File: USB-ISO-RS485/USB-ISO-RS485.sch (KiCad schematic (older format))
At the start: 36 parts, among them P1 RS485 Connector, P10 TST, P11 TST, P12 TST, P13 UART Interface, P2 USB_A, P3 TST, P4 TST, P5 TST, P6 TST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

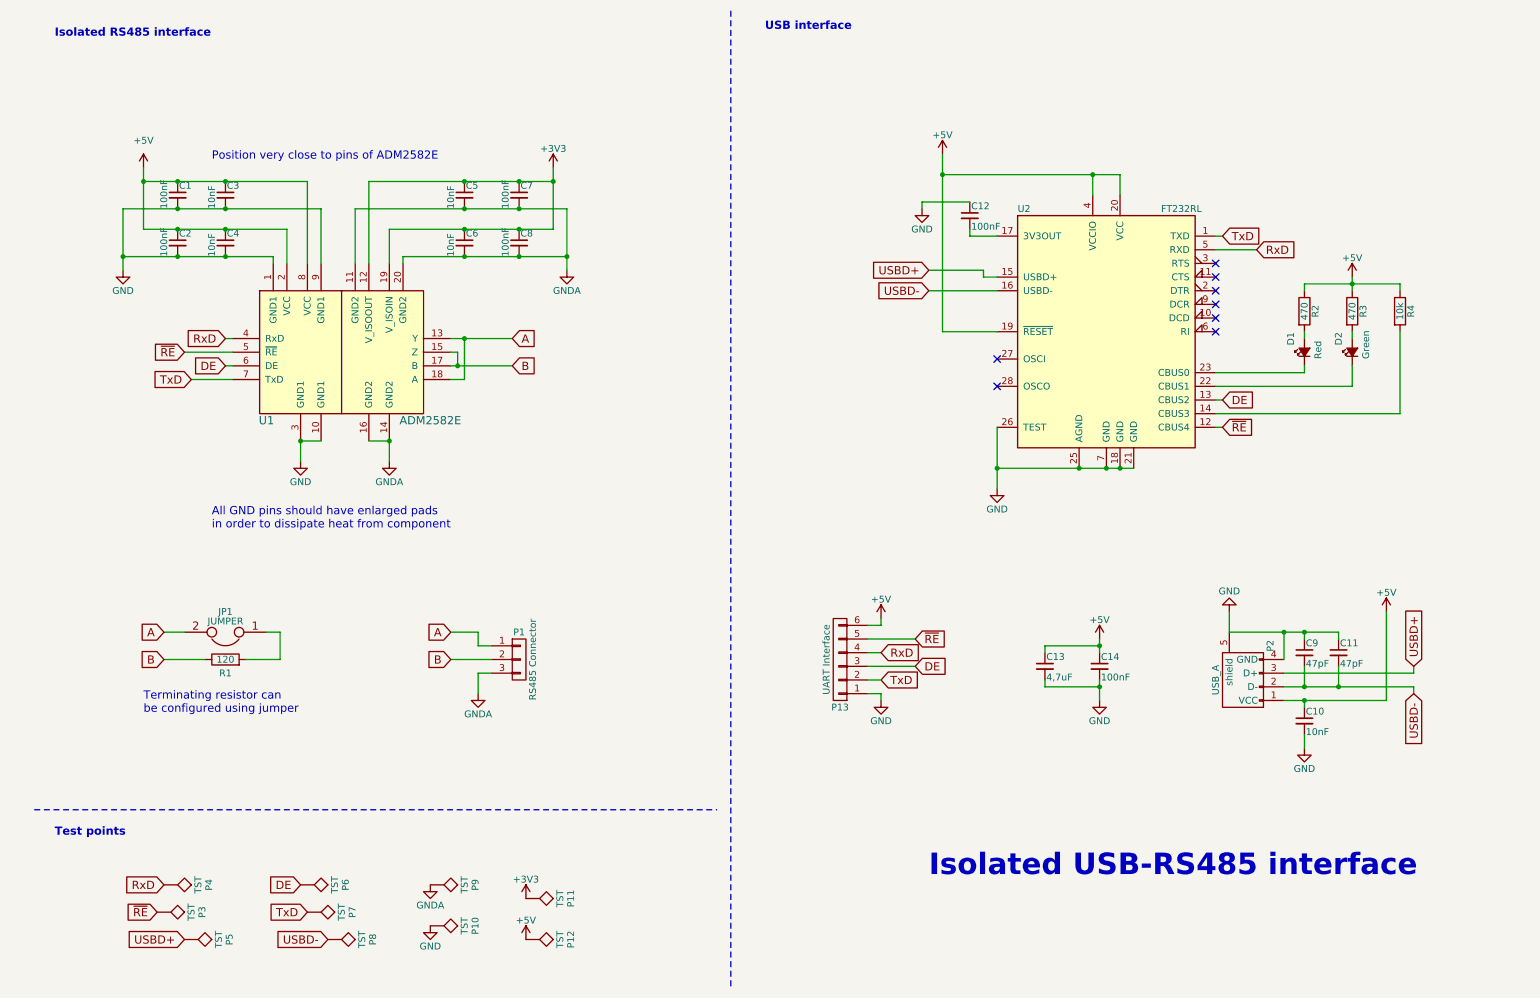
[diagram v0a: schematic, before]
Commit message: assigned all footprints
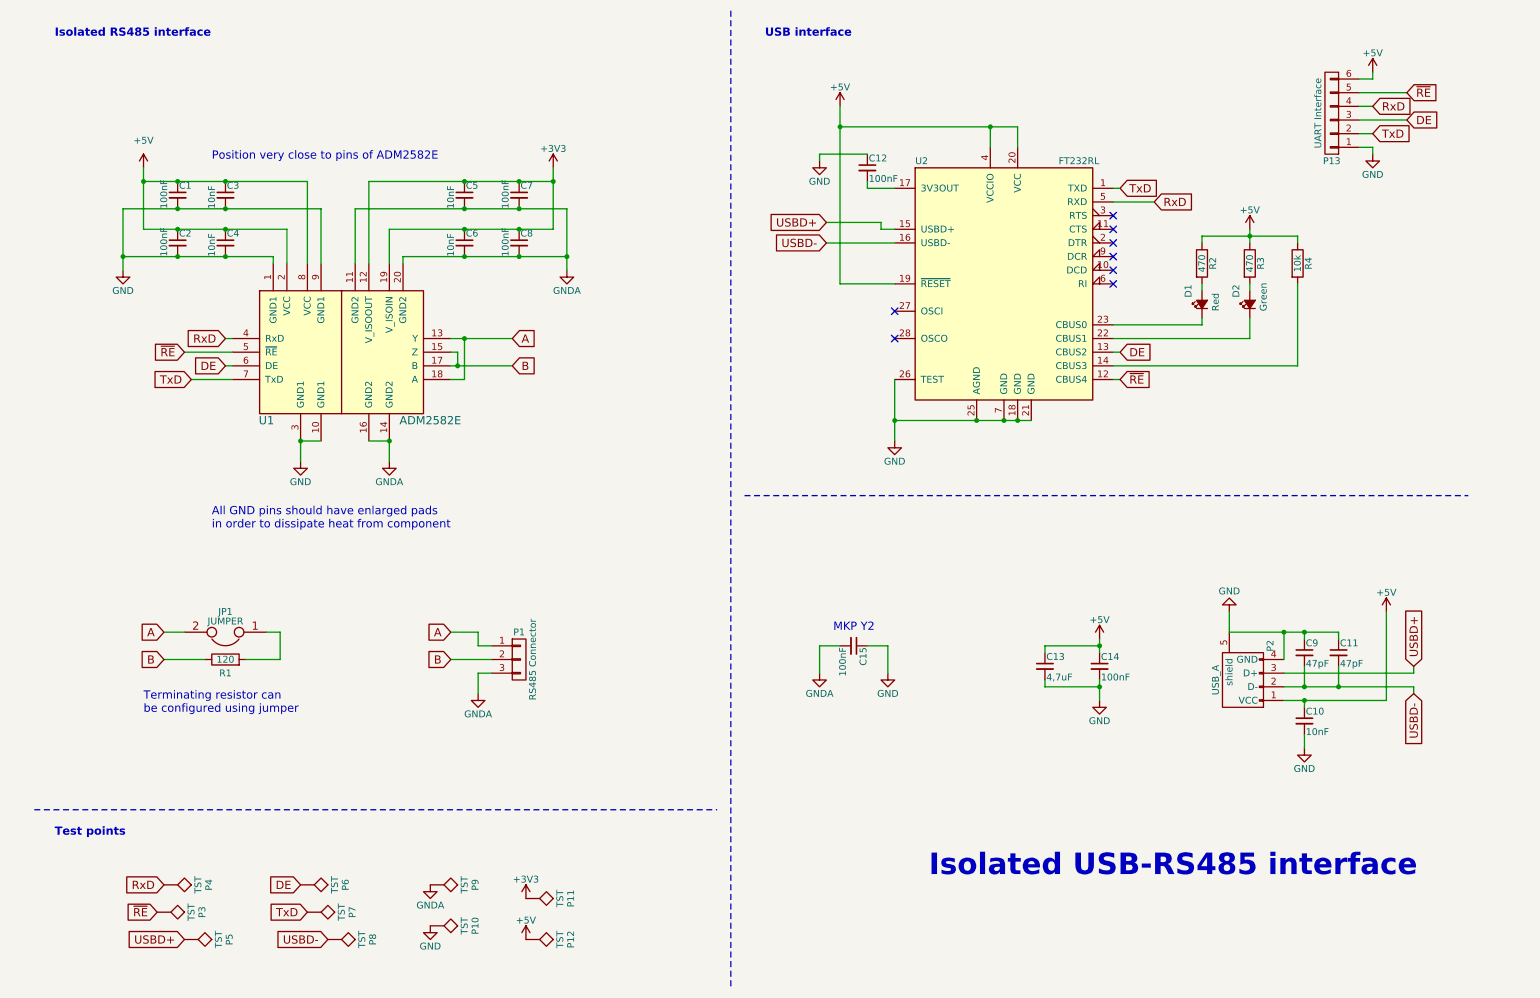
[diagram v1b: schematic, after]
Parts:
- added C15: 100nF, Capacitors_THT:C_Rect_L26.5mm_W7.0mm_P22.50mm_MKS4, symbol C_Small
- C1, C10, C11, C12, C13, C14, C2, C3, C4, C5, C6, C7, C8, C9: footprint (none) -> Capacitors_SMD:C_0805_HandSoldering
- D1, D2: footprint (none) -> LEDs:LED_0805
- JP1: footprint (none) -> Pin_Headers:Pin_Header_Straight_1x02_Pitch2.54mm
- P1: footprint (none) -> Connectors_WAGO:WAGO_734_3pin_Straight_RuggedPads
- P10, P11, P12, P3, P4, P5, P6, P7, P8, P9: footprint (none) -> Measurement_Points:Test_Point_Keystone_5010-5014_Multipurpose
- P13: footprint (none) -> Pin_Headers:Pin_Header_Straight_1x06_Pitch2.54mm
- P2: footprint (none) -> Connectors:USB_B
- R1, R2, R3, R4: footprint (none) -> Resistors_SMD:R_0805_HandSoldering
- U1: footprint Housings_SOIC:SOIC-20W_7.5x12.8mm_Pitch1.27mm -> ADM2582E:ADM2582E-SOIC20W-Thermal
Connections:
- net GND: now also C15.1
- net GNDA: now also C15.2
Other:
- note added: "MKP Y2"
- moved on the sheet: C12, D1, D2, P13, R2, R3, R4, U2

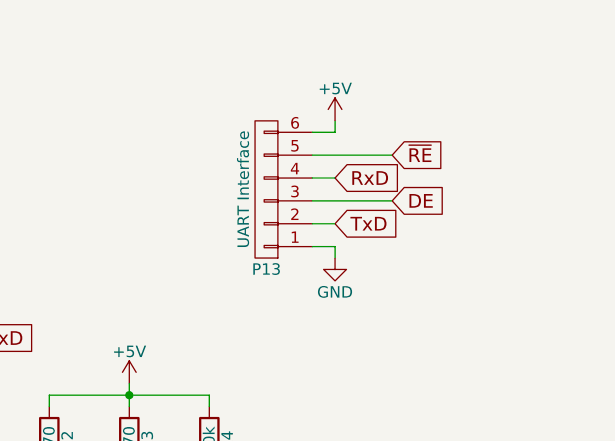
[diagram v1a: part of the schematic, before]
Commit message: broken layout - ADM2582E footprint to narrow
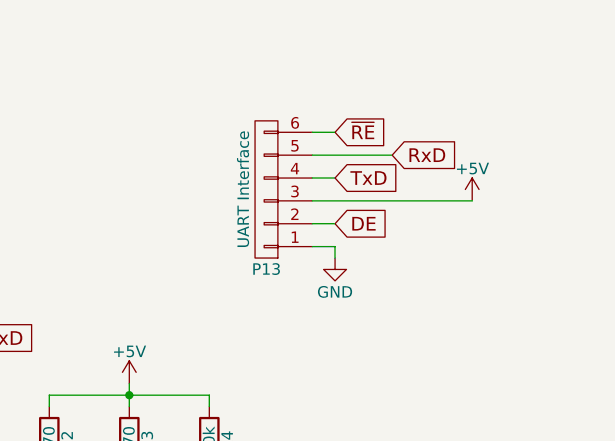
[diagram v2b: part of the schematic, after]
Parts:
- P10, P11, P12, P3, P4, P5, P6, P7, P8, P9: footprint Measurement_Points:Test_Point_Keystone_5010-5014_Multipurpose -> Measurement_Points:Measurement_Point_Round-TH_Small
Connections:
- net +5V: now also P13.3 (P3); no longer P13.6 (P6)
- net DE: now also P13.2 (P2); no longer P13.3 (P3)
- net RxD: now also P13.5 (P5); no longer P13.4 (P4)
- net TxD: now also P13.4 (P4); no longer P13.2 (P2)
- net ~RE: now also P13.6 (P6); no longer P13.5 (P5)
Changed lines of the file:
@@
 F 0 "P5" H 1700 7650 50  0000 C BNN
 F 1 "TST" H 1700 7600 50  0000 C CNN
-F 2 "Measurement_Points:Test_Point_Keystone_5010-5014_Multipurpose" H 1700 7350 60  0001 C CNN
+F 2 "Measurement_Points:Measurement_Point_Round-TH_Small" H 1700 7350 60  0001 C CNN
 F 3 "" H 1700 7350 60  0000 C CNN
 	1    1700 7350
@@
 F 0 "P8" H 2750 7650 50  0000 C BNN
 F 1 "TST" H 2750 7600 50  0000 C CNN
-F 2 "Measurement_Points:Test_Point_Keystone_5010-5014_Multipurpose" H 2750 7350 60  0001 C CNN
+F 2 "Measurement_Points:Measurement_Point_Round-TH_Small" H 2750 7350 60  0001 C CNN
 F 3 "" H 2750 7350 60  0000 C CNN
 	1    2750 7350
@@
 F 0 "P4" H 1550 7250 50  0000 C BNN
 F 1 "TST" H 1550 7200 50  0000 C CNN
-F 2 "Measurement_Points:Test_Point_Keystone_5010-5014_Multipurpose" H 1550 6950 60  0001 C CNN
+F 2 "Measurement_Points:Measurement_Point_Round-TH_Small" H 1550 6950 60  0001 C CNN
 F 3 "" H 1550 6950 60  0000 C CNN
 	1    1550 6950
@@
 F 0 "P3" H 1500 7450 50  0000 C BNN
 F 1 "TST" H 1500 7400 50  0000 C CNN
-F 2 "Measurement_Points:Test_Point_Keystone_5010-5014_Multipurpose" H 1500 7150 60  0001 C CNN
+F 2 "Measurement_Points:Measurement_Point_Round-TH_Small" H 1500 7150 60  0001 C CNN
 F 3 "" H 1500 7150 60  0000 C CNN
 	1    1500 7150
@@
 F 0 "P6" H 2550 7250 50  0000 C BNN
 F 1 "TST" H 2550 7200 50  0000 C CNN
-F 2 "Measurement_Points:Test_Point_Keystone_5010-5014_Multipurpose" H 2550 6950 60  0001 C CNN
+F 2 "Measurement_Points:Measurement_Point_Round-TH_Small" H 2550 6950 60  0001 C CNN
 F 3 "" H 2550 6950 60  0000 C CNN
 	1    2550 6950
@@
 F 0 "P7" H 2600 7450 50  0000 C BNN
 F 1 "TST" H 2600 7400 50  0000 C CNN
-F 2 "Measurement_Points:Test_Point_Keystone_5010-5014_Multipurpose" H 2600 7150 60  0001 C CNN
+F 2 "Measurement_Points:Measurement_Point_Round-TH_Small" H 2600 7150 60  0001 C CNN
 F 3 "" H 2600 7150 60  0000 C CNN
 	1    2600 7150
@@
 F 0 "P9" H 3500 7250 50  0000 C BNN
 F 1 "TST" H 3500 7200 50  0000 C CNN
-F 2 "Measurement_Points:Test_Point_Keystone_5010-5014_Multipurpose" H 3500 6950 60  0001 C CNN
+F 2 "Measurement_Points:Measurement_Point_Round-TH_Small" H 3500 6950 60  0001 C CNN
 F 3 "" H 3500 6950 60  0000 C CNN
 	1    3500 6950
@@
 F 0 "P11" H 4200 7350 50  0000 C BNN
 F 1 "TST" H 4200 7300 50  0000 C CNN
-F 2 "Measurement_Points:Test_Point_Keystone_5010-5014_Multipurpose" H 4200 7050 60  0001 C CNN
+F 2 "Measurement_Points:Measurement_Point_Round-TH_Small" H 4200 7050 60  0001 C CNN
 F 3 "" H 4200 7050 60  0000 C CNN
 	1    4200 7050
@@
 F 0 "P10" H 3500 7550 50  0000 C BNN
 F 1 "TST" H 3500 7500 50  0000 C CNN
-F 2 "Measurement_Points:Test_Point_Keystone_5010-5014_Multipurpose" H 3500 7250 60  0001 C CNN
+F 2 "Measurement_Points:Measurement_Point_Round-TH_Small" H 3500 7250 60  0001 C CNN
 F 3 "" H 3500 7250 60  0000 C CNN
 	1    3500 7250
@@
 F 0 "P12" H 4200 7650 50  0000 C BNN
 F 1 "TST" H 4200 7600 50  0000 C CNN
-F 2 "Measurement_Points:Test_Point_Keystone_5010-5014_Multipurpose" H 4200 7350 60  0001 C CNN
+F 2 "Measurement_Points:Measurement_Point_Round-TH_Small" H 4200 7350 60  0001 C CNN
 F 3 "" H 4200 7350 60  0000 C CNN
 	1    4200 7350
@@
 Wire Notes Line
 	600  6400 5600 6400
+Text GLabel 10400 1250 2    60   Input ~ 0
+TxD
+Text GLabel 10650 1150 2    60   Input ~ 0
+RxD
 Text GLabel 10400 1450 2    60   Input ~ 0
-TxD
-Text GLabel 10400 1250 2    60   Input ~ 0
-RxD
-Text GLabel 10650 1350 2    60   Input ~ 0
 DE
-Text GLabel 10650 1150 2    60   Input ~ 0
+Text GLabel 10400 1050 2    60   Input ~ 0
 ~RE
 $Comp
@@
 L +5V #PWR022
 U 1 1 590F657C
-P 10400 1000
-F 0 "#PWR022" H 10400 850 50  0001 C CNN
-F 1 "+5V" H 10400 1140 50  0000 C CNN
-F 2 "" H 10400 1000 60  0000 C CNN
-F 3 "" H 10400 1000 60  0000 C CNN
-	1    10400 1000
+P 11000 1350
+F 0 "#PWR022" H 11000 1200 50  0001 C CNN
+F 1 "+5V" H 11000 1490 50  0000 C CNN
+F 2 "" H 11000 1350 60  0000 C CNN
+F 3 "" H 11000 1350 60  0000 C CNN
+	1    11000 1350
 	1    0    0    -1
 $EndComp
@@
 	10400 1550 10400 1600
 Wire Wire Line
-	10300 1050 10400 1050
-Wire Wire Line
-	10400 1050 10400 1000
-Wire Wire Line
-	10300 1150 10650 1150
-Wire Wire Line
-	10300 1250 10400 1250
-Wire Wire Line
-	10300 1350 10650 1350
-Wire Wire Line
-	10300 1450 10400 1450
-Wire Wire Line
 	9750 5500 10700 5500
 Wire Wire Line
@@
 Text Notes 6450 5100 0    60   ~ 0
 MKP Y2
+Wire Wire Line
+	10300 1150 10650 1150
+Wire Wire Line
+	10300 1250 10400 1250
+Wire Wire Line
+	10300 1350 11000 1350
+Wire Wire Line
+	10300 1450 10400 1450
+Wire Wire Line
+	10300 1050 10400 1050
 $EndSCHEMATC

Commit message: added corrected footprint, rerouted board
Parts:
- U1: footprint ADM2582E:ADM2582E-SOIC20W-Thermal -> ADM2582E:ADM2582E-SOIC20W-Thermal-Correct
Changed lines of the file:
@@
 F 0 "U1" H 2300 2550 60  0000 C CNN
 F 1 "ADM2582E" H 3500 2550 60  0000 C CNN
-F 2 "ADM2582E:ADM2582E-SOIC20W-Thermal" H 3100 3050 60  0001 C CNN
+F 2 "ADM2582E:ADM2582E-SOIC20W-Thermal-Correct" H 3100 3050 60  0001 C CNN
 F 3 "" H 3100 3050 60  0001 C CNN
 	1    2850 3050

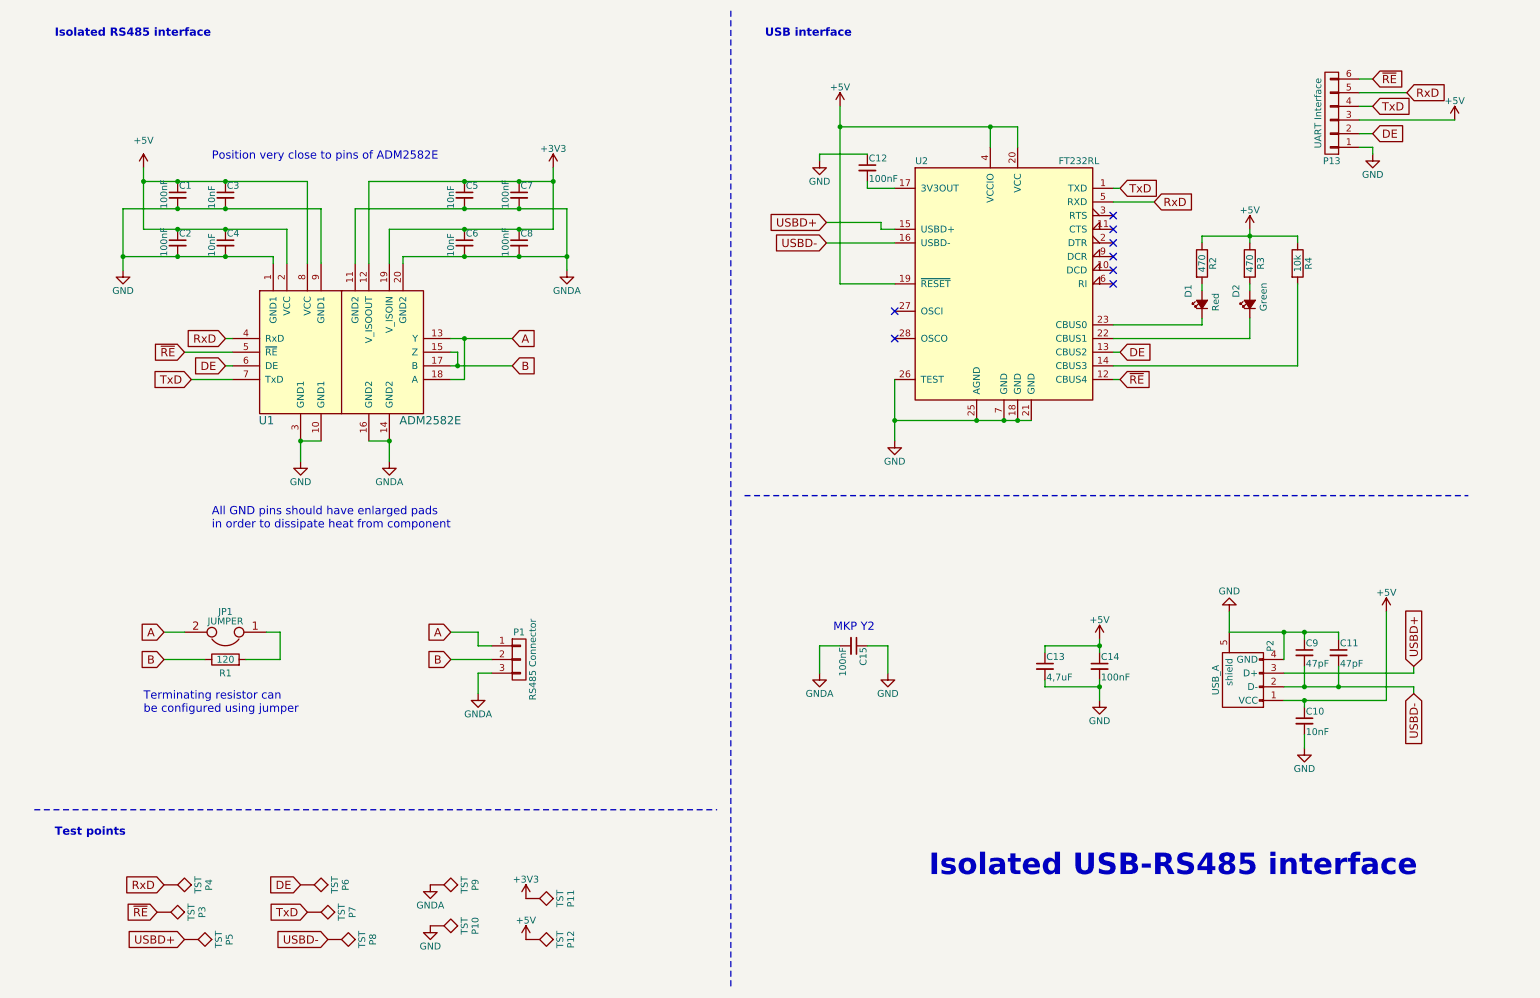
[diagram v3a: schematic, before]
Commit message: added switching USB power, shielding separated, added TVS & EMI filter on USB line
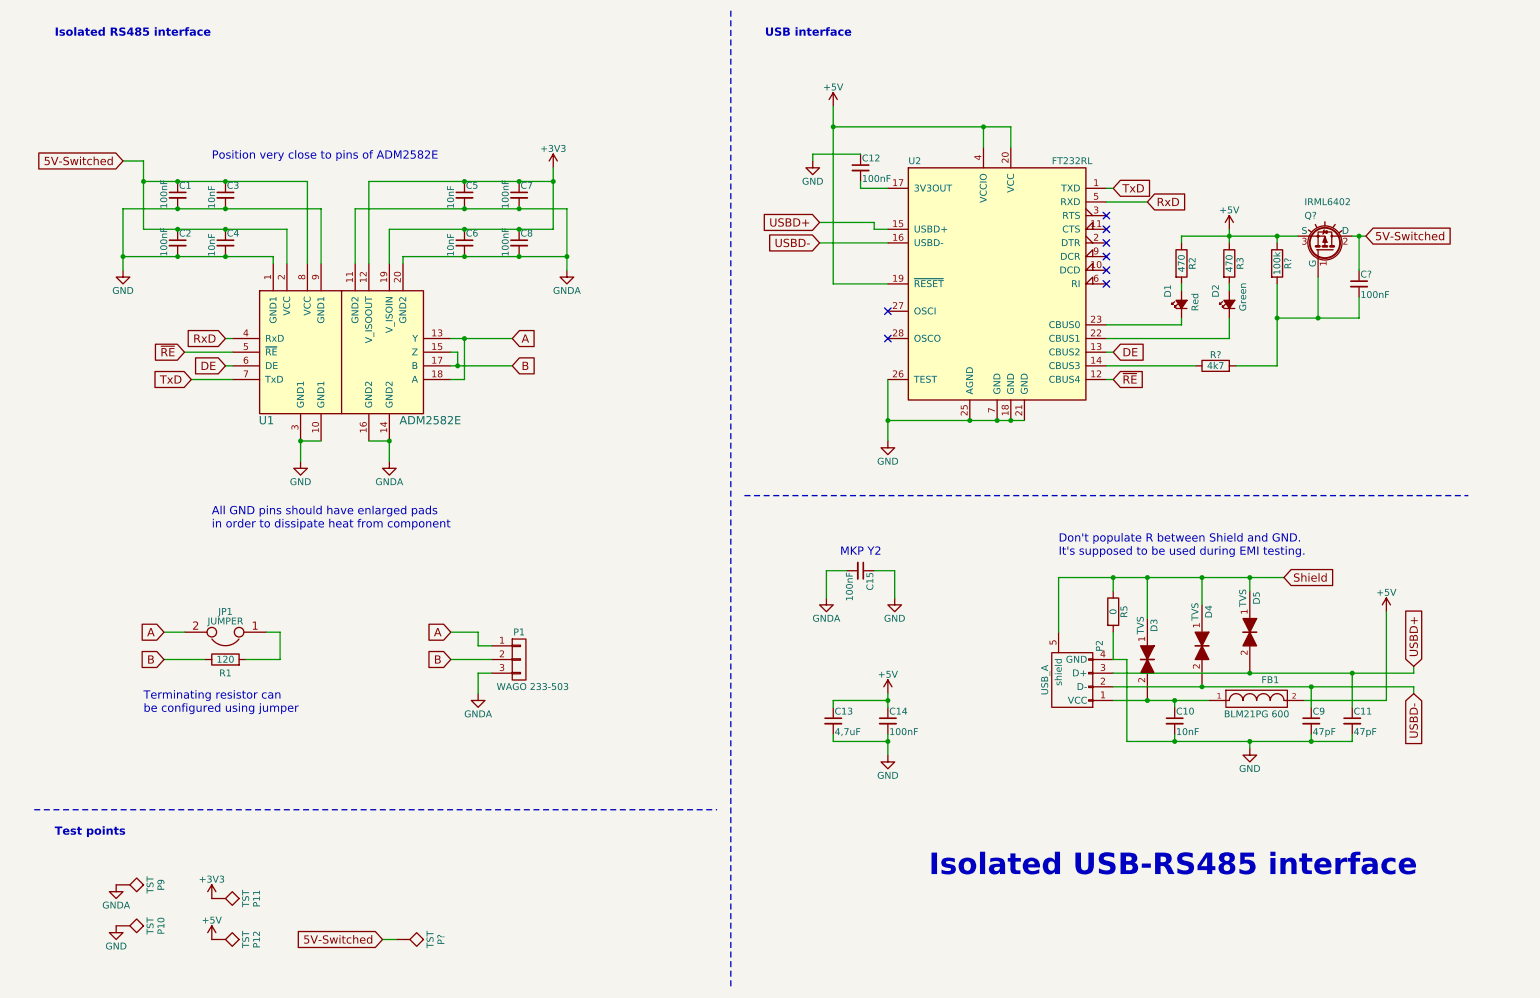
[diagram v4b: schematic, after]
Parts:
- removed P13: UART Interface, Pin_Headers:Pin_Header_Straight_1x06_Pitch2.54mm, symbol CONN_01X06
- removed P3, P4, P5, P6, P7, P8: TST, Measurement_Points:Measurement_Point_Round-TH_Small, symbol TST
- removed R4: 10k, Resistors_SMD:R_0805_HandSoldering, symbol R
- added C?: 100nF, Capacitors_SMD:C_0805_HandSoldering, symbol C_Small
- added D3, D4, D5: TVS, symbol TVS
- added FB1: BLM21PG 600, symbol FILTER
- added P?: TST, Measurement_Points:Measurement_Point_Round-TH_Small, symbol TST
- added Q?: IRML6402, symbol IRF9540N
- added R5: 0, symbol R
- added R?: 4k7, Resistors_SMD:R_0805_HandSoldering, symbol R
- added R?: 100k, Resistors_SMD:R_0805_HandSoldering, symbol R
- P1: value RS485 Connector -> WAGO 233-503
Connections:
- net +5V: now also FB1.2, Q?.3 (S), R?.1; no longer C1.1, C10.1, C2.1, C3.1, C4.1, P2.1 (VCC), U1.2 (VCC), U1.8 (VCC)
- net GND: now also C11.2, C9.2, R5.2; no longer C11.1, C9.1, P2.5 (shield)
- net USBD+: now also C11.1, D5.2
- net USBD-: now also C9.1, D4.2; no longer C11.2, C9.2
- net at U2.14 (CBUS3): now also R?.1
- new net: C10.1, D3.2, FB1.1, P2.1 (VCC)
- new net: C?.2, Q?.1 (G), R?.2, R?.2
- new net 5V-Switched: C1.1, C2.1, C3.1, C4.1, C?.1, P?.1, Q?.2 (D), U1.2 (VCC), U1.8 (VCC)
- new net Shield: D3.1, D4.1, D5.1, P2.5 (shield), R5.1
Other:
- note added: "Don't populate R between Shield and GND.\nIt's supposed to be used during EMI testing.\n"
- moved on the sheet: C10, C11, C12, C13, C14, C15, C9, D1, D2, P10, P11, P12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
